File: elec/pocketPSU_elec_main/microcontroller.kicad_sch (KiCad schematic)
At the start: 16 parts, among them J1 Conn_01x20_Pin, SW3 TS-1187A-B-A-B, SW6 TS-1187A-B-A-B, U2 ESP32-S3-WROOM-1(N16R2), U3 AMS1117-3.3, U5 F.0603.00026/P2-0603B1TS2-06T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

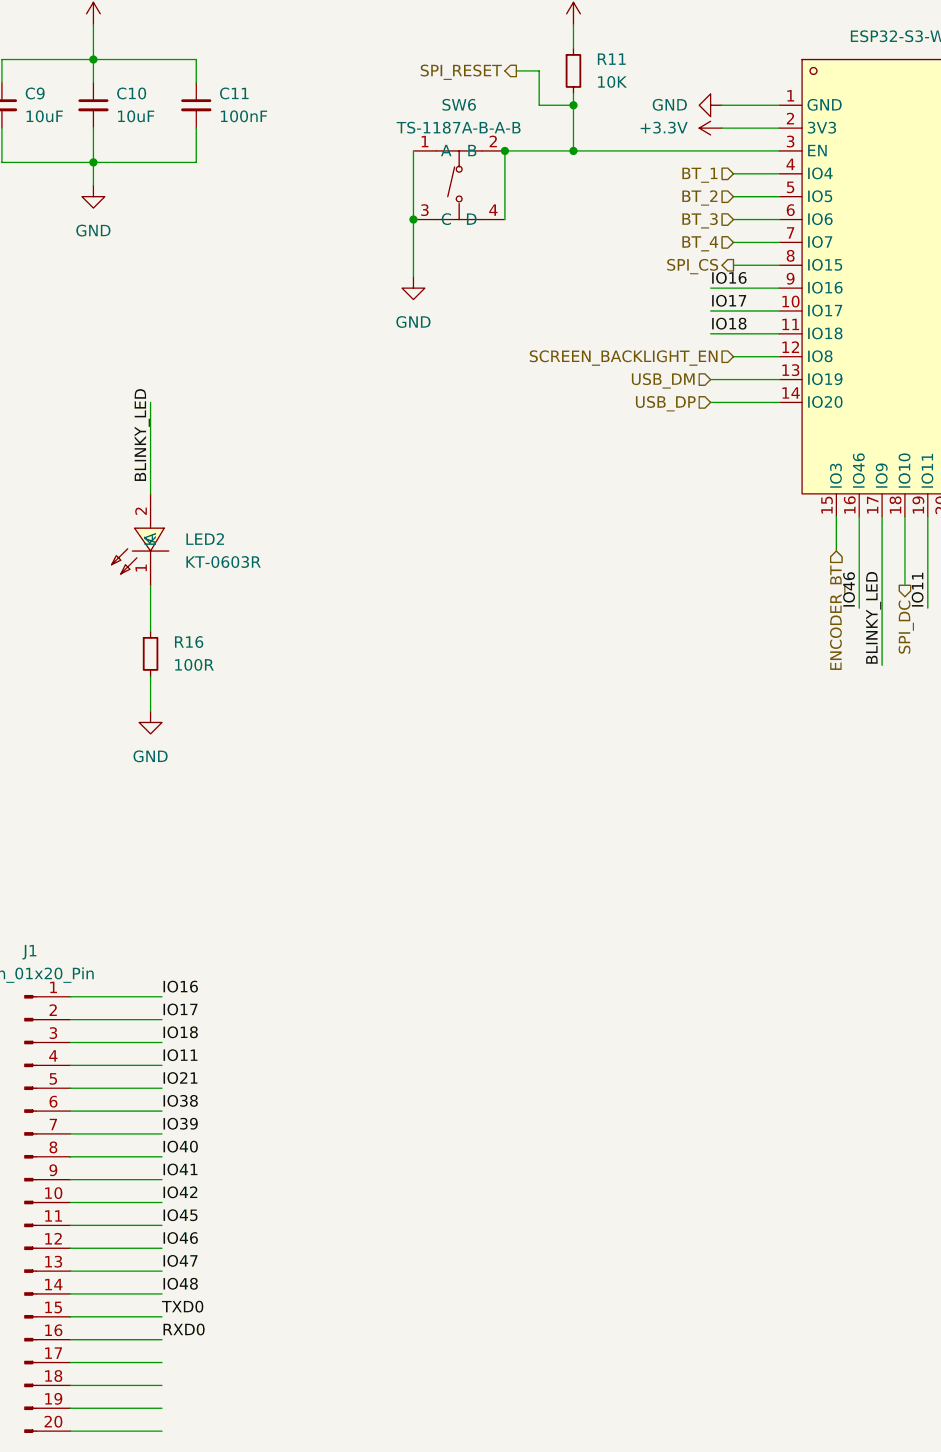
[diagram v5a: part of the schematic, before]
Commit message: add buttons and leds for on/off indication
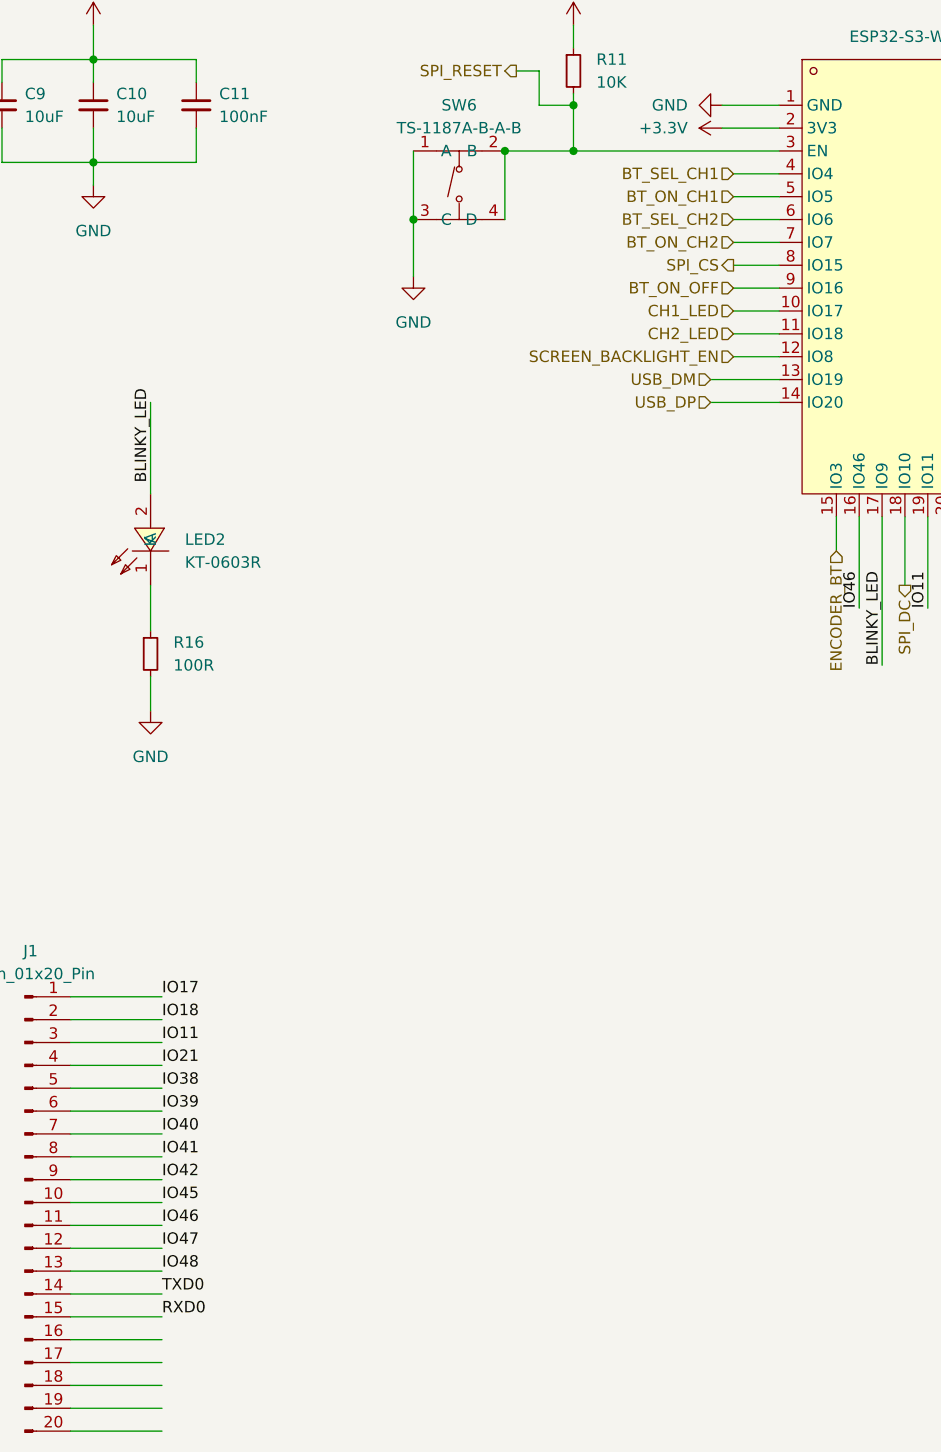
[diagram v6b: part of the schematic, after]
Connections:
- net IO11: now also J1.3 (Pin_3); no longer J1.4 (Pin_4)
- net IO17: now also J1.1 (Pin_1); no longer J1.2 (Pin_2), U2.10 (IO17)
- net IO18: now also J1.2 (Pin_2); no longer J1.3 (Pin_3), U2.11 (IO18)
- net IO21: now also J1.4 (Pin_4); no longer J1.5 (Pin_5)
- net IO38: now also J1.5 (Pin_5); no longer J1.6 (Pin_6)
- net IO39: now also J1.6 (Pin_6); no longer J1.7 (Pin_7)
- net IO40: now also J1.7 (Pin_7); no longer J1.8 (Pin_8)
- net IO41: now also J1.8 (Pin_8); no longer J1.9 (Pin_9)
- net IO42: now also J1.9 (Pin_9); no longer J1.10 (Pin_10)
- net IO45: now also J1.10 (Pin_10); no longer J1.11 (Pin_11)
- net IO46: now also J1.11 (Pin_11); no longer J1.12 (Pin_12)
- net IO47: now also J1.12 (Pin_12); no longer J1.13 (Pin_13)
- net IO48: now also J1.13 (Pin_13); no longer J1.14 (Pin_14)
- net RXD0: now also J1.15 (Pin_15); no longer J1.16 (Pin_16)
- net TXD0: now also J1.14 (Pin_14); no longer J1.15 (Pin_15)
- net BT_1 renamed BT_SEL_CH1
- net BT_2 renamed BT_ON_CH1
- net BT_3 renamed BT_SEL_CH2
- net BT_4 renamed BT_ON_CH2
- net IO16 renamed BT_ON_OFF
- net BT_ON_OFF: no longer J1.1 (Pin_1)
- new net CH1_LED: U2.10 (IO17)
- new net CH2_LED: U2.11 (IO18)

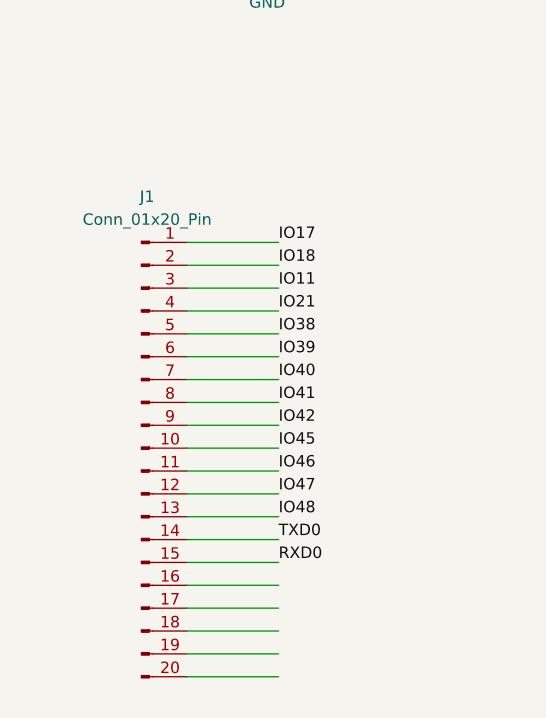
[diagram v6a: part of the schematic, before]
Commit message: move pullup nodes, change to 2.54mm header
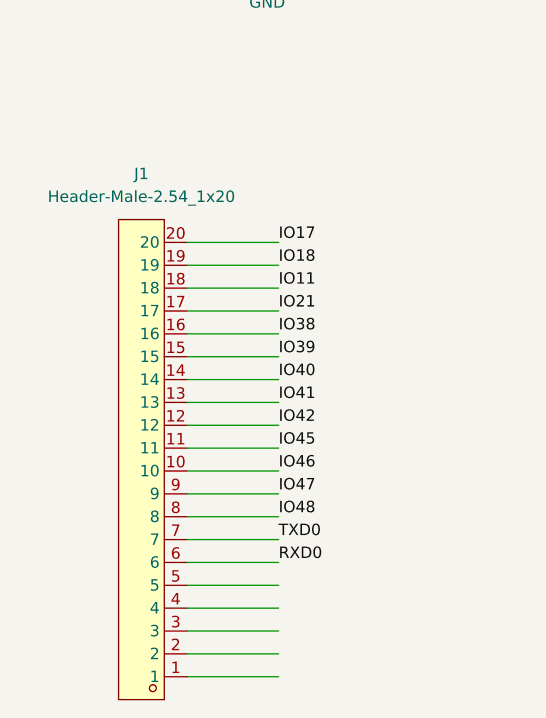
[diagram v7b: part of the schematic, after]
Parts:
- removed J1: Conn_01x20_Pin, Connector_PinHeader_1.27mm:PinHeader_1x20_P1.27mm_Vertical, symbol Connector:Conn_01x20_Pin
- added J1: Header-Male-2.54_1x20, footprints:HDR-TH_20P-P2.54-V-M-1, symbol footprints:Header-Male-2.54_1x20
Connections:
- net IO11: now also J1.18
- net IO17: now also J1.20
- net IO18: now also J1.19
- net IO21: now also J1.17
- net IO38: now also J1.16
- net IO39: now also J1.15
- net IO40: now also J1.14
- net IO41: now also J1.13
- net IO42: now also J1.12
- net IO45: now also J1.11
- net IO46: now also J1.10
- net IO47: now also J1.9
- net IO48: now also J1.8
- net RXD0: now also J1.6
- net TXD0: now also J1.7
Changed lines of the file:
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@@
 	)
 	(symbol
-		(lib_id "Connector:Conn_01x20_Pin")
-		(at 33.02 160.02 0)
+		(lib_id "footprints:Header-Male-2.54_1x20")
+		(at 33.02 161.29 180)
 		(unit 1)
 		(exclude_from_sim no)
@@
 		(fields_autoplaced yes)
 		(property "Reference" "J1"
-			(at 33.655 132.08 0)
+			(at 33.02 129.54 0)
 			(effects
 				(font
@@
 			)
 		)
-		(property "Value" "Conn_01x20_Pin"
-			(at 33.655 134.62 0)
+		(property "Value" "Header-Male-2.54_1x20"
+			(at 33.02 132.08 0)
 			(effects
 				(font
@@
 			)
 		)
-		(property "Footprint" "Connector_PinHeader_1.27mm:PinHeader_1x20_P1.27mm_Vertical"
-			(at 33.02 160.02 0)
+		(property "Footprint" "footprints:HDR-TH_20P-P2.54-V-M-1"
+			(at 33.02 129.54 0)
 			(effects
 				(font
@@
 			)
 		)
-		(property "Datasheet" "~"
-			(at 33.02 160.02 0)
+		(property "Datasheet" "https://lcsc.com/product-detail/Male-Header_2-54mm-1-20P-Straight-Headers-Pins_C50981.html"
+			(at 33.02 127 0)
 			(effects
 				(font
@@
 			)
 		)
-		(property "Description" "Generic connector, single row, 01x20, script generated"
-			(at 33.02 160.02 0)
+		(property "Description" ""
+			(at 33.02 161.29 0)
 			(effects
 				(font
@@
 			)
 		)
-		(pin "17"
-		)
-		(pin "11"
-		)
-		(pin "14"
+		(property "LCSC Part" "C50981"
+			(at 33.02 124.46 0)
+			(effects
+				(font
+					(size 1.27 1.27)
+				)
+				(hide yes)
+			)
 		)
 		(pin "2"
 		)
-		(pin "8"
+		(pin "20"
+		)
+		(pin "1"
+		)
+		(pin "13"
 		)
 		(pin "9"
+		)
+		(pin "12"
 		)
 		(pin "5"
@@
 		(pin "7"
 		)
+		(pin "8"
+		)
+		(pin "3"
+		)
 		(pin "4"
-		)
-		(pin "1"
 		)
 		(pin "10"
 		)
-		(pin "12"
+		(pin "16"
 		)
-		(pin "20"
+		(pin "17"
 		)
-		(pin "3"
+		(pin "11"
+		)
+		(pin "18"
+		)
+		(pin "19"
 		)
 		(pin "15"
 		)
-		(pin "18"
-		)
-		(pin "13"
-		)
-		(pin "19"
-		)
-		(pin "16"
+		(pin "14"
 		)
 		(instances

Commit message: board routed
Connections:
- net GND: now also SW3.4 (D), SW6.4 (D); no longer SW3.1 (A), SW6.1 (A)
- net SPI_RESET: now also SW6.1 (A); no longer SW6.4 (D)
- net at R18.2, SW3.2 (B), U2.27 (IO0): now also SW3.1 (A); no longer SW3.4 (D)
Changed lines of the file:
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@@
 	)
 	(junction
-		(at 93.98 38.1)
+		(at 177.8 87.63)
 		(diameter 0)
 		(color 0 0 0 0)
 	)
 	(junction
-		(at 171.45 35.56)
+		(at 93.98 38.1)
 		(diameter 0)
 		(color 0 0 0 0)
 	)
 	(junction
-		(at 182.88 77.47)
+		(at 166.37 71.12)
 		(diameter 0)
 		(color 0 0 0 0)
 	)
 	(junction
-		(at 40.64 33.02)
+		(at 171.45 35.56)
 		(diameter 0)
 		(color 0 0 0 0)
 	)
 	(junction
-		(at 40.64 44.45)
+		(at 81.28 55.88)
 		(diameter 0)
 		(color 0 0 0 0)
 	)
 	(junction
-		(at 76.2 50.8)
+		(at 40.64 33.02)
 		(diameter 0)
 		(color 0 0 0 0)
 	)
 	(junction
-		(at 187.96 71.12)
+		(at 40.64 44.45)
 		(diameter 0)
 		(color 0 0 0 0)
 	)
 	(junction
-		(at 86.36 43.18)
+		(at 187.96 71.12)
 		(diameter 0)
 		(color 0 0 0 0)
 	)
 	(junction
-		(at 172.72 85.09)
+		(at 218.44 76.2)
 		(diameter 0)
 		(color 0 0 0 0)
 	)
 	(junction
-		(at 218.44 76.2)
+		(at 93.98 43.18)
 		(diameter 0)
 		(color 0 0 0 0)
 	)
 	(junction
-		(at 93.98 43.18)
+		(at 87.63 43.18)
 		(diameter 0)
 		(color 0 0 0 0)
@@
 	(wire
 		(pts
-			(xy 76.2 50.8) (xy 76.2 57.15)
+			(xy 81.28 55.88) (xy 81.28 57.15)
 		)
 		(stroke
@@
 	(wire
 		(pts
-			(xy 172.72 77.47) (xy 172.72 85.09)
-		)
-		(stroke
-			(width 0)
-			(type default)
-		)
-	)
-	(wire
-		(pts
 			(xy 171.45 35.56) (xy 173.99 35.56)
 		)
@@
 	(wire
 		(pts
+			(xy 81.28 55.88) (xy 76.2 55.88)
+		)
+		(stroke
+			(width 0)
+			(type default)
+		)
+	)
+	(wire
+		(pts
 			(xy 140.97 83.82) (xy 140.97 91.44)
 		)
@@
 	(wire
 		(pts
+			(xy 166.37 71.12) (xy 187.96 71.12)
+		)
+		(stroke
+			(width 0)
+			(type default)
+		)
+	)
+	(wire
+		(pts
 			(xy 52.07 44.45) (xy 40.64 44.45)
 		)
@@
 	(wire
 		(pts
+			(xy 182.88 85.09) (xy 182.88 87.63)
+		)
+		(stroke
+			(width 0)
+			(type default)
+		)
+	)
+	(wire
+		(pts
 			(xy 241.3 57.15) (xy 241.3 60.96)
 		)
@@
 	(wire
 		(pts
+			(xy 86.36 55.88) (xy 81.28 55.88)
+		)
+		(stroke
+			(width 0)
+			(type default)
+		)
+	)
+	(wire
+		(pts
 			(xy 157.48 58.42) (xy 173.99 58.42)
 		)
@@
 	(wire
 		(pts
-			(xy 219.71 39.37) (xy 228.6 39.37)
+			(xy 166.37 77.47) (xy 166.37 71.12)
 		)
 		(stroke
@@
 	(wire
 		(pts
-			(xy 111.76 66.04) (xy 116.84 66.04)
+			(xy 219.71 39.37) (xy 228.6 39.37)
 		)
 		(stroke
@@
 	(wire
 		(pts
-			(xy 130.81 83.82) (xy 130.81 91.44)
+			(xy 111.76 66.04) (xy 116.84 66.04)
 		)
 		(stroke
@@
 	(wire
 		(pts
-			(xy 86.36 43.18) (xy 86.36 50.8)
+			(xy 130.81 83.82) (xy 130.81 91.44)
 		)
 		(stroke
@@
 	(wire
 		(pts
+			(xy 86.36 50.8) (xy 86.36 55.88)
+		)
+		(stroke
+			(width 0)
+			(type default)
+		)
+	)
+	(wire
+		(pts
 			(xy 110.49 40.64) (xy 116.84 40.64)
 		)
@@
 	(wire
 		(pts
+			(xy 177.8 87.63) (xy 172.72 87.63)
+		)
+		(stroke
+			(width 0)
+			(type default)
+		)
+	)
+	(wire
+		(pts
 			(xy 38.1 170.18) (xy 48.26 170.18)
 		)
@@
 	(wire
 		(pts
-			(xy 86.36 43.18) (xy 93.98 43.18)
+			(xy 86.36 43.18) (xy 87.63 43.18)
+		)
+		(stroke
+			(width 0)
+			(type default)
+		)
+	)
+	(wire
+		(pts
+			(xy 177.8 87.63) (xy 177.8 91.44)
+		)
+		(stroke
+			(width 0)
+			(type default)
+		)
+	)
+	(wire
+		(pts
+			(xy 87.63 36.83) (xy 87.63 43.18)
 		)
 		(stroke
@@
 	(wire
 		(pts
+			(xy 172.72 77.47) (xy 166.37 77.47)
+		)
+		(stroke
+			(width 0)
+			(type default)
+		)
+	)
+	(wire
+		(pts
 			(xy 38.1 185.42) (xy 48.26 185.42)
 		)
@@
 	(wire
 		(pts
-			(xy 182.88 77.47) (xy 182.88 85.09)
-		)
-		(stroke
-			(width 0)
-			(type default)
-		)
-	)
-	(wire
-		(pts
 			(xy 111.76 60.96) (xy 116.84 60.96)
 		)
@@
 	(wire
 		(pts
-			(xy 157.48 71.12) (xy 187.96 71.12)
+			(xy 76.2 36.83) (xy 87.63 36.83)
+		)
+		(stroke
+			(width 0)
+			(type default)
+		)
+	)
+	(wire
+		(pts
+			(xy 87.63 43.18) (xy 93.98 43.18)
+		)
+		(stroke
+			(width 0)
+			(type default)
+		)
+	)
+	(wire
+		(pts
+			(xy 157.48 71.12) (xy 166.37 71.12)
 		)
 		(stroke
@@
 	(wire
 		(pts
+			(xy 76.2 43.18) (xy 76.2 36.83)
+		)
+		(stroke
+			(width 0)
+			(type default)
+		)
+	)
+	(wire
+		(pts
 			(xy 52.07 33.02) (xy 40.64 33.02)
 		)
@@
 	(wire
 		(pts
+			(xy 182.88 87.63) (xy 177.8 87.63)
+		)
+		(stroke
+			(width 0)
+			(type default)
+		)
+	)
+	(wire
+		(pts
 			(xy 210.82 66.04) (xy 210.82 68.58)
 		)
@@
 	(wire
 		(pts
-			(xy 76.2 43.18) (xy 76.2 50.8)
+			(xy 135.89 83.82) (xy 135.89 91.44)
 		)
 		(stroke
@@
 	(wire
 		(pts
-			(xy 135.89 83.82) (xy 135.89 91.44)
+			(xy 46.99 91.44) (xy 46.99 96.52)
 		)
 		(stroke
@@
 	(wire
 		(pts
-			(xy 46.99 91.44) (xy 46.99 96.52)
+			(xy 40.64 44.45) (xy 40.64 46.99)
 		)
 		(stroke
@@
 	(wire
 		(pts
-			(xy 40.64 44.45) (xy 40.64 46.99)
+			(xy 76.2 55.88) (xy 76.2 50.8)
 		)
 		(stroke
@@
 	(wire
 		(pts
-			(xy 172.72 85.09) (xy 172.72 91.44)
+			(xy 172.72 85.09) (xy 172.72 87.63)
 		)
 		(stroke
@@
 	(symbol
 		(lib_id "power:GND")
-		(at 172.72 91.44 0)
+		(at 177.8 91.44 0)
 		(unit 1)
 		(exclude_from_sim no)
@@
 		(fields_autoplaced yes)
 		(property "Reference" "#PWR070"
-			(at 172.72 97.79 0)
+			(at 177.8 97.79 0)
 			(effects
 				(font
@@
 		)
 		(property "Value" "GND"
-			(at 172.72 96.52 0)
+			(at 177.8 96.52 0)
 			(effects
 				(font
@@
 		)
 		(property "Footprint" ""
-			(at 172.72 91.44 0)
+			(at 177.8 91.44 0)
 			(effects
 				(font
@@
 		)
 		(property "Datasheet" ""
-			(at 172.72 91.44 0)
+			(at 177.8 91.44 0)
 			(effects
 				(font
@@
 		)
 		(property "Description" "Power symbol creates a global label with name \"GND\" , ground"
-			(at 172.72 91.44 0)
+			(at 177.8 91.44 0)
 			(effects
 				(font
@@
 	(symbol
 		(lib_id "power:GND")
-		(at 76.2 57.15 0)
+		(at 81.28 57.15 0)
 		(unit 1)
 		(exclude_from_sim no)
@@
 		(fields_autoplaced yes)
 		(property "Reference" "#PWR030"
-			(at 76.2 63.5 0)
+			(at 81.28 63.5 0)
 			(effects
 				(font
@@
 		)
 		(property "Value" "GND"
-			(at 76.2 62.23 0)
+			(at 81.28 62.23 0)
 			(effects
 				(font
@@
 		)
 		(property "Footprint" ""
-			(at 76.2 57.15 0)
+			(at 81.28 57.15 0)
 			(effects
 				(font
@@
 		)
 		(property "Datasheet" ""
-			(at 76.2 57.15 0)
+			(at 81.28 57.15 0)
 			(effects
 				(font
@@
 		)
 		(property "Description" "Power symbol creates a global label with name \"GND\" , ground"
-			(at 76.2 57.15 0)
+			(at 81.28 57.15 0)
 			(effects
 				(font
